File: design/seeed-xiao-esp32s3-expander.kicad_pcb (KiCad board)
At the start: 2 copper layers, 17.8 x 14 mm, 12 parts, among them J1 Conn_01x07, J2 Conn_01x07, J3 30pin, J4 Conn_01x02, J5 Conn_01x01

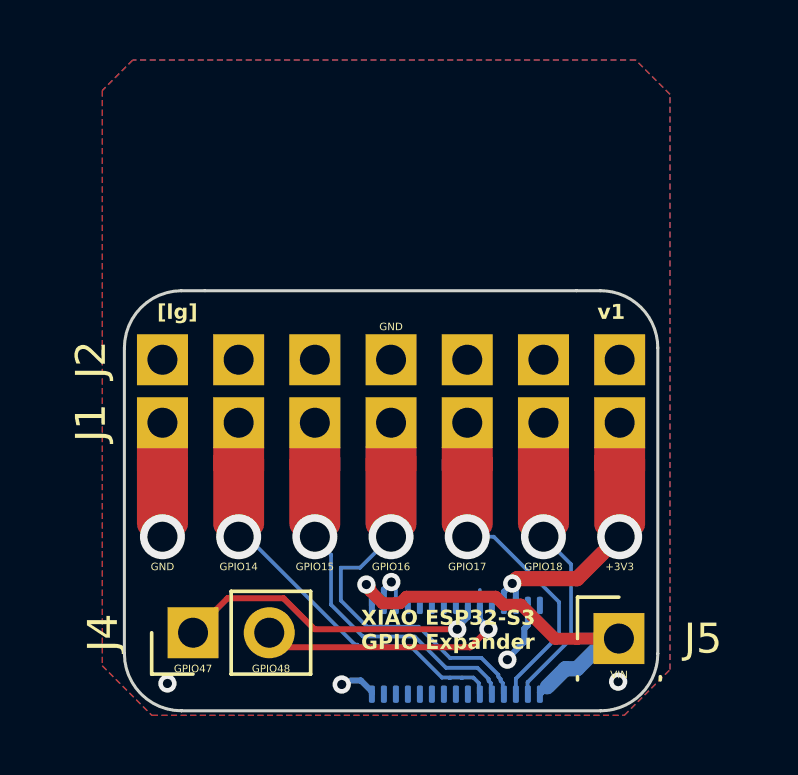
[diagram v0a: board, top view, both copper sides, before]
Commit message: Add min clearances and fix in pcb
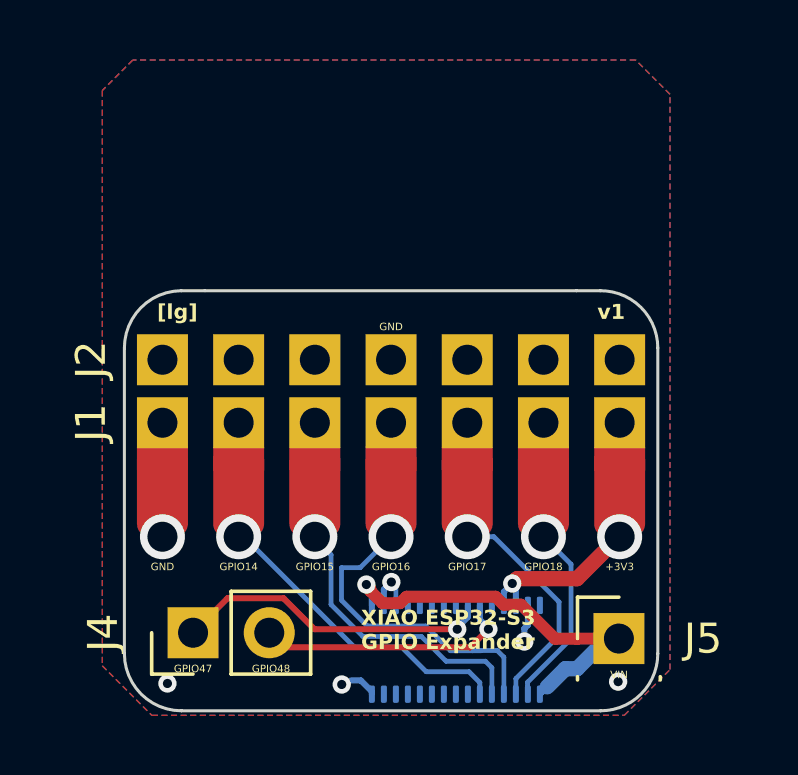
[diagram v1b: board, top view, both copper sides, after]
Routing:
- net GND: track 4.76 -> 3.92 mm
- net GPIO48: track 9.18 -> 8.67 mm
